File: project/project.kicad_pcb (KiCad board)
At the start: 4 copper layers, 84 x 41 mm, 142 parts, among them J101 Front, J102 FFC, SW101 SW_DIP_x04, U101 GX101, U201 74HC595, U301 74HC595, U401 74HC595, U501 74HC595

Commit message: fixing silkscreen typo
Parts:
- removed kibuzzard-6981884A: G***, kibuzzard-6981884A
- added kibuzzard-698AEBE9: G***, kibuzzard-698AEBE9, B.Cu at (178.3, 105.5)

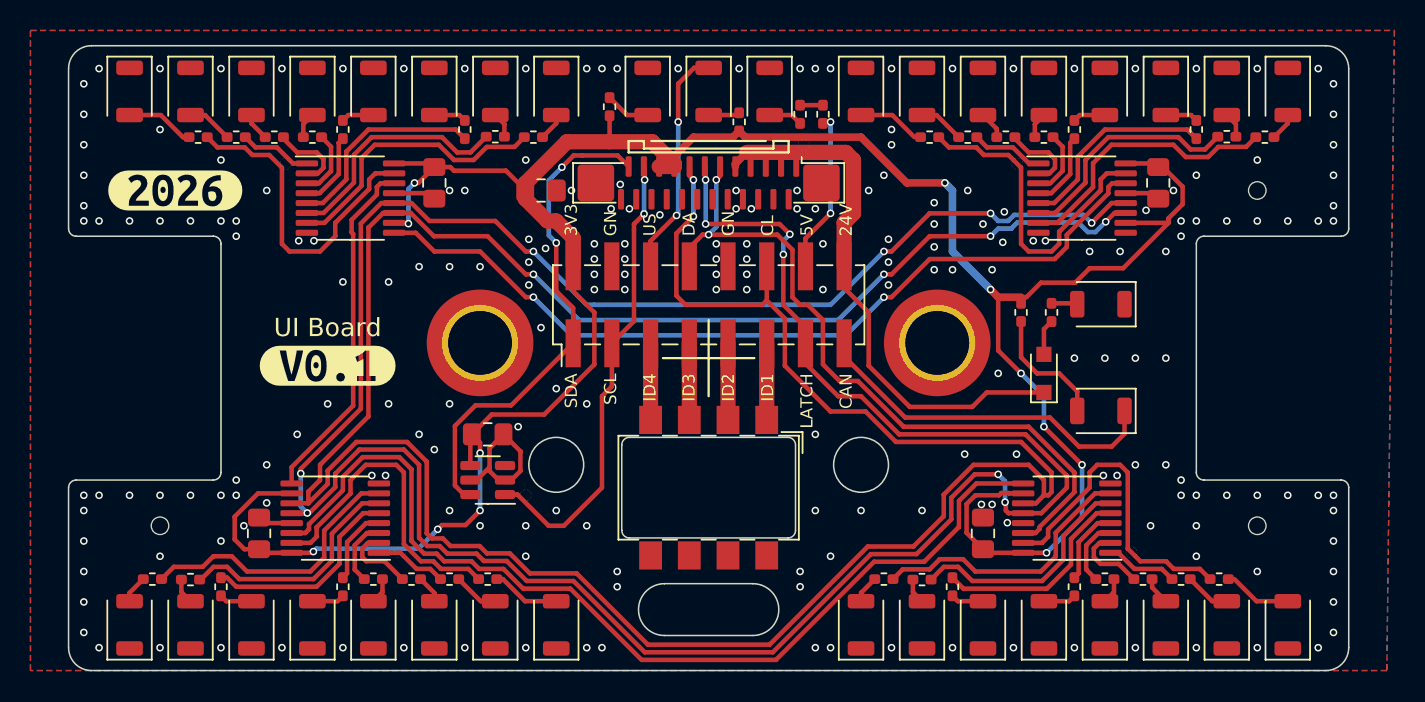
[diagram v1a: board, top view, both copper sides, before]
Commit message: updating kibot,fixing silkscreen, lowering led current
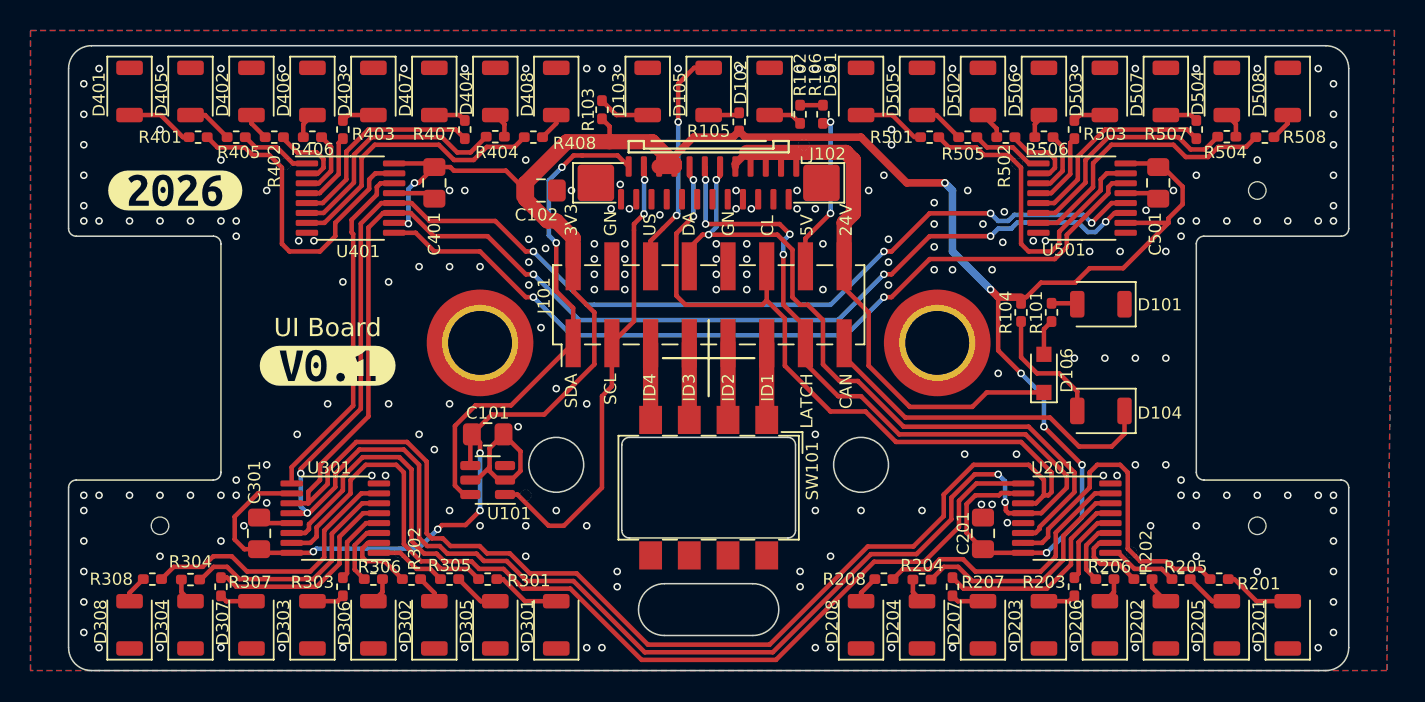
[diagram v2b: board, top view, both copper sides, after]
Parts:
- R201, R202, R203, R204, R205, R206, R207, R208, R301, R302, R303, R304, R305, R306, R307, R308, R401, R402, R403, R404, R405, R406, R407, R408, R501, R502, R503, R504, R505, R506, R507, R508: value 220R -> 330R
- moved R103 0.54 mm to (161.3, 74.7)

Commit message: parts consolidation and small fixes
* Inverting input LEDs
* Switching to TMP102 as TMP101 is no longer available
* Helping 74HC forget state after power loss
* bumping up version
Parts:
- removed REF** (x3): toolhole, -local:toolhole
- removed kibuzzard-69816F1E: G***, kibuzzard-69816F1E
- added R107: 330R, Resistor_SMD:R_0402_1005Metric_Pad0.72x0.64mm_HandSolder, F.Cu at (157.8, 78.8)
- added kibuzzard-69BC5702: G***, kibuzzard-69BC5702, F.Cu at (145.3, 96.0)
- U101: value GX101 -> TMP102; footprint Package_TO_SOT_SMD:SOT-23-6 -> -local:SOT-563
- moved R102 2.55 mm to (174.8, 72.5), turned to 90 degrees
- moved R106 1.00 mm to (174.8, 75.0)
- moved C102 0.50 mm to (157.3, 80.5)
- moved R103 0.23 mm to (161.4, 74.5)
- turned D102 to 90 degrees
- turned D103 to 90 degrees
- turned D105 to 90 degrees
- turned D201 to -90 degrees
- turned D202 to -90 degrees
- turned D203 to -90 degrees
- turned D204 to -90 degrees
- turned D205 to -90 degrees
- turned D206 to -90 degrees
- turned D207 to -90 degrees
- turned D208 to -90 degrees
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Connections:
- D201 pad 1: GND -> /driver1/Ar
- D201 pad 2: /driver1/Ar -> 3V3
- D202 pad 1: GND -> /driver1/Cr
- D202 pad 2: /driver1/Cr -> 3V3
- D203 pad 1: GND -> /driver1/Er
- D203 pad 2: /driver1/Er -> 3V3
- D204 pad 1: GND -> /driver1/Gr
- D204 pad 2: /driver1/Gr -> 3V3
- D205 pad 1: GND -> /driver1/Br
- D205 pad 2: /driver1/Br -> 3V3
- D206 pad 1: GND -> /driver1/Dr
- D206 pad 2: /driver1/Dr -> 3V3
- D207 pad 1: GND -> /driver1/Fr
- D207 pad 2: /driver1/Fr -> 3V3
- D208 pad 1: GND -> /driver1/Hr
- D208 pad 2: /driver1/Hr -> 3V3
- D301 pad 1: GND -> /driver2/Ar
- D301 pad 2: /driver2/Ar -> 3V3
- D302 pad 1: GND -> /driver2/Cr
- D302 pad 2: /driver2/Cr -> 3V3
- D303 pad 1: GND -> /driver2/Er
- D303 pad 2: /driver2/Er -> 3V3
- D304 pad 1: GND -> /driver2/Gr
- D304 pad 2: /driver2/Gr -> 3V3
- D305 pad 1: GND -> /driver2/Br
- D305 pad 2: /driver2/Br -> 3V3
- D306 pad 1: GND -> /driver2/Dr
- D306 pad 2: /driver2/Dr -> 3V3
- D307 pad 1: GND -> /driver2/Fr
- D307 pad 2: /driver2/Fr -> 3V3
- D308 pad 1: GND -> /driver2/Hr
- D308 pad 2: /driver2/Hr -> 3V3
- D401 pad 1: GND -> /driver3/Ar
- D401 pad 2: /driver3/Ar -> 3V3
- D402 pad 1: GND -> /driver3/Cr
- D402 pad 2: /driver3/Cr -> 3V3
- D403 pad 1: GND -> /driver3/Er
- D403 pad 2: /driver3/Er -> 3V3
- D404 pad 1: GND -> /driver3/Gr
- D404 pad 2: /driver3/Gr -> 3V3
- D405 pad 1: GND -> /driver3/Br
- D405 pad 2: /driver3/Br -> 3V3
- D406 pad 1: GND -> /driver3/Dr
- D406 pad 2: /driver3/Dr -> 3V3
- D407 pad 1: GND -> /driver3/Fr
- D407 pad 2: /driver3/Fr -> 3V3
- D408 pad 1: GND -> /driver3/Hr
- D408 pad 2: /driver3/Hr -> 3V3
- D501 pad 1: GND -> /driver4/Ar
- D501 pad 2: /driver4/Ar -> 3V3
- D502 pad 1: GND -> /driver4/Cr
- D502 pad 2: /driver4/Cr -> 3V3
- D503 pad 1: GND -> /driver4/Er
- D503 pad 2: /driver4/Er -> 3V3
- D504 pad 1: GND -> /driver4/Gr
- D504 pad 2: /driver4/Gr -> 3V3
- D505 pad 1: GND -> /driver4/Br
- D505 pad 2: /driver4/Br -> 3V3
- D506 pad 1: GND -> /driver4/Dr
- D506 pad 2: /driver4/Dr -> 3V3
- D507 pad 1: GND -> /driver4/Fr
- D507 pad 2: /driver4/Fr -> 3V3
- D508 pad 1: GND -> /driver4/Hr
- D508 pad 2: /driver4/Hr -> 3V3
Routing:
- net 3V3: track 168.4 -> 311.7 mm, vias 12 -> 14
- net USR_LED: track 15.2 -> 12.4 mm
- net Net-(D105-Pad2): track 2.06 -> 4.34 mm
- net SDA: track 32.7 -> 31.9 mm
- net Net-(D103-Pad2): track 3.39 -> 3.97 mm
- net SCL: track 30.5 -> 31.1 mm
- net GND: track 17.1 -> 17.6 mm, vias 218 -> 189
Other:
- board text added: "WormControl Input32 UI Board"
- board text removed: "UI Board"

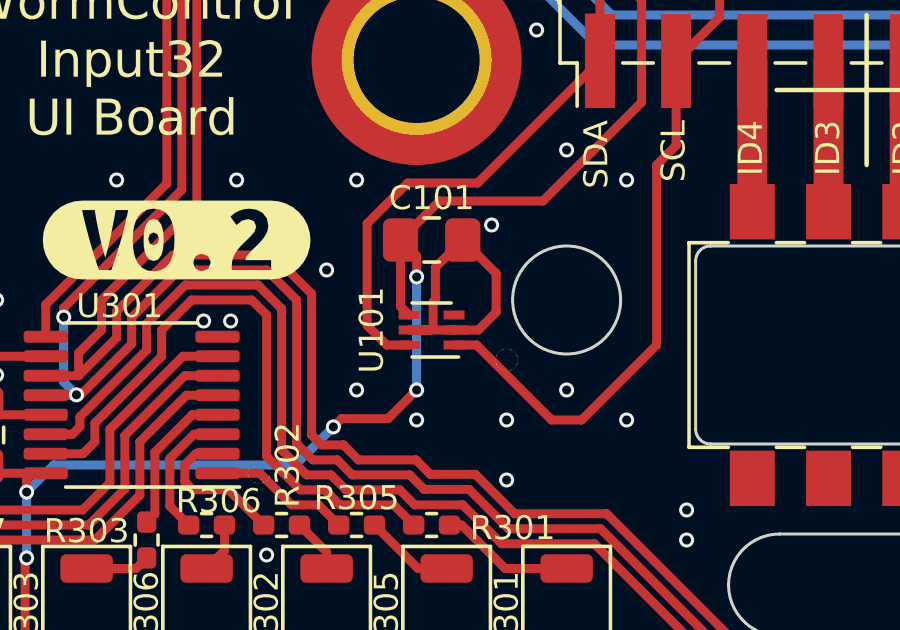
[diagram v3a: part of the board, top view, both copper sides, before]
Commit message: fixing tmp102 pinout
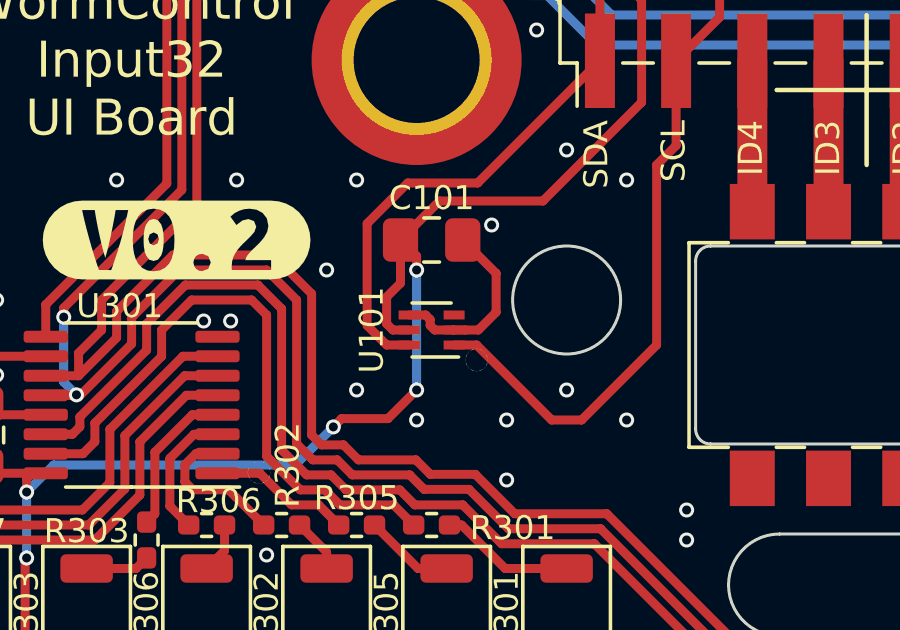
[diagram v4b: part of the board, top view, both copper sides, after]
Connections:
- U101 pad 4: 3V3 -> GND
- U101 pad 5: GND -> 3V3
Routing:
- net GND: track 17.6 -> 13.7 mm
- net 3V3: track 311.7 -> 312.9 mm
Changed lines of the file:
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@@
     )
     (fp_text value "G***" (at 0 4.36087) (layer "F.SilkS") hide
-      (effects (font (size 0 0)))
+      (effects (font (size 0 0) (thickness 0.15)))
     )
     (fp_poly (pts
@@
       (net 1 "unconnected-(U101-Pad3)") (pinfunction "ALERT") (pintype "open_collector+no_connect"))
     (pad "4" smd rect (at 0.75 0.5 180) (size 0.7 0.3) (layers "F.Cu" "F.Paste" "F.Mask")
-      (net 2 "3V3") (pinfunction "V+") (pintype "power_in"))
-    (pad "5" smd rect (at 0.75 0 180) (size 0.7 0.3) (layers "F.Cu" "F.Paste" "F.Mask")
       (net 3 "GND") (pinfunction "ADD0") (pintype "input"))
+    (pad "5" smd rect (at 0.75 0 180) (size 0.7 0.3) (layers "F.Cu" "F.Paste" "F.Mask")
+      (net 2 "3V3") (pinfunction "V+") (pintype "power_in"))
     (pad "6" smd rect (at 0.75 -0.5 180) (size 0.7 0.3) (layers "F.Cu" "F.Paste" "F.Mask")
       (net 45 "SDA") (pinfunction "SDA") (pintype "bidirectional"))
@@
   (gr_line (start 163.0125 76.7875) (end 163.0125 77.5375) (layer "F.SilkS") (width 0.15))
   (gr_circle (center 174.5125 77.0375) (end 174.512501 77.0375) (layer "F.SilkS") (width 0.75) (fill none))
-  (gr_circle (center 156.2625 100.0375) (end 156.262501 100.0375) (layer "F.SilkS") (width 0.75) (fill none))
+  (gr_circle (center 155.2625 100.0375) (end 155.262501 100.0375) (layer "F.SilkS") (width 0.75) (fill none))
   (gr_circle (center 196.0125 103.7875) (end 196.012501 103.7875) (layer "F.SilkS") (width 0.75) (fill none))
   (gr_line (start 172.5125 76.7875) (end 172.5125 77.2875) (layer "F.SilkS") (width 0.15))
@@
     (style (thickness 0.15) (arrow_length 1.27) (text_position_mode 0) (extension_height 0.58642) (extension_offset 0.5) keep_text_aligned)
   )
-  (segment (start 153.2625 96.575) (end 152.725 96.0375) (width 0.3) (layer "F.Cu") (net 2))
   (segment (start 150.2625 110.0875) (end 154.2625 110.0875) (width 0.5) (layer "F.Cu") (net 2))
   (segment (start 187.315656 100.0375) (end 185.7625 100.0375) (width 0.3) (layer "F.Cu") (net 2))
@@
   (segment (start 154.2625 71.9875) (end 158.2625 71.9875) (width 0.5) (layer "F.Cu") (net 2))
   (segment (start 166.0125 77.7875) (end 166.0125 78.4625) (width 0.5) (layer "F.Cu") (net 2))
+  (segment (start 153.2625 97.0375) (end 153.2625 96.575) (width 0.3) (layer "F.Cu") (net 2))
   (segment (start 188.2625 106.762) (end 188.2625 110.0375) (width 0.3) (layer "F.Cu") (net 2))
   (segment (start 138.2625 110.0875) (end 140.2125 110.0875) (width 0.5) (layer "F.Cu") (net 2))
@@
   (segment (start 160.7625 91.4475) (end 160.7625 88.0375) (width 0.3) (layer "F.Cu") (net 2))
   (segment (start 152.725 96.0375) (end 154.025 94.7375) (width 0.3) (layer "F.Cu") (net 2))
+  (segment (start 153.0125 99.0375) (end 152.469606 99.0375) (width 0.3) (layer "F.Cu") (net 2))
   (segment (start 185.1875 100.6125) (end 185.1875 102.5) (width 0.3) (layer "F.Cu") (net 2))
   (segment (start 130.2625 110.0875) (end 134.2625 110.0875) (width 0.5) (layer "F.Cu") (net 2))
@@
   (segment (start 139 103.8125) (end 138.7625 103.575) (width 0.3) (layer "F.Cu") (net 2))
   (segment (start 198.073529 78.5) (end 199.3625 79.788971) (width 0.3) (layer "F.Cu") (net 2))
+  (segment (start 152.469606 99.0375) (end 152.2625 98.830394) (width 0.3) (layer "F.Cu") (net 2))
   (segment (start 161.7625 76.8375) (end 158.633724 76.8375) (width 1) (layer "F.Cu") (net 2))
-  (segment (start 153.2625 97.26875) (end 153.2625 96.575) (width 0.3) (layer "F.Cu") (net 2))
   (segment (start 188.7625 87.0375) (end 187.2625 87.0375) (width 0.5) (layer "F.Cu") (net 2))
   (segment (start 138.7625 103.575) (end 137.8 103.575) (width 0.3) (layer "F.Cu") (net 2))
@@
   (segment (start 142.2625 71.9875) (end 146.2625 71.9875) (width 0.5) (layer "F.Cu") (net 2))
   (segment (start 160.7625 88.0375) (end 159.3725 86.6475) (width 0.3) (layer "F.Cu") (net 2))
+  (segment (start 153.2625 96.575) (end 152.725 96.0375) (width 0.3) (layer "F.Cu") (net 2))
   (segment (start 137.1625 102.9375) (end 137.1625 101.438972) (width 0.3) (layer "F.Cu") (net 2))
   (segment (start 147.625 78.2625) (end 150.025 78.2625) (width 0.3) (layer "F.Cu") (net 2))
   (segment (start 194.2625 110.0875) (end 190.2625 110.0875) (width 0.5) (layer "F.Cu") (net 2))
   (segment (start 175.9625 72.8375) (end 175.9625 76.3375) (width 0.5) (layer "F.Cu") (net 2))
+  (segment (start 152.2625 98.830394) (end 152.2625 97.9375) (width 0.3) (layer "F.Cu") (net 2))
   (segment (start 152.308339 101.991661) (end 150.7625 101.991661) (width 0.3) (layer "F.Cu") (net 2))
   (segment (start 206.2625 71.9875) (end 202.2625 71.9875) (width 0.5) (layer "F.Cu") (net 2))
+  (segment (start 152.725 97.475) (end 152.725 96.0375) (width 0.3) (layer "F.Cu") (net 2))
   (segment (start 140.2625 104.438) (end 140.2625 103.99375) (width 0.3) (layer "F.Cu") (net 2))
   (segment (start 154.9625 78.7375) (end 156.225 80) (width 0.3) (layer "F.Cu") (net 2))
@@
   (segment (start 146.2625 110.0875) (end 150.2625 110.0875) (width 0.5) (layer "F.Cu") (net 2))
   (segment (start 164.5625 76.8375) (end 161.7625 76.8375) (width 1) (layer "F.Cu") (net 2))
-  (segment (start 152.725 98.25) (end 152.725 96.0375) (width 0.3) (layer "F.Cu") (net 2))
+  (segment (start 152.2625 97.9375) (end 152.725 97.475) (width 0.3) (layer "F.Cu") (net 2))
   (segment (start 188.7625 87.0375) (end 189.113972 87.0375) (width 0.3) (layer "F.Cu") (net 2))
   (segment (start 150.2625 71.9875) (end 154.2625 71.9875) (width 0.5) (layer "F.Cu") (net 2))
   (segment (start 188.9 103.8125) (end 186.5 103.8125) (width 0.3) (layer "F.Cu") (net 2))
   (segment (start 186.2625 71.9875) (end 182.2625 71.9875) (width 0.5) (layer "F.Cu") (net 2))
-  (segment (start 153.0125 98.5375) (end 152.725 98.25) (width 0.3) (layer "F.Cu") (net 2))
   (segment (start 187.2625 87.0375) (end 186.7625 86.5375) (width 0.5) (layer "F.Cu") (net 2))
   (segment (start 170.2625 76.135) (end 170.665 76.5375) (width 0.5) (layer "F.Cu") (net 2))
@@
   (via (at 186.7625 86.5375) (size 0.5) (drill 0.3) (layers "F.Cu" "B.Cu") (net 2))
   (via (at 140.2625 104.438) (size 0.5) (drill 0.3) (layers "F.Cu" "B.Cu") (net 2))
-  (via (at 153.2625 97.26875) (size 0.5) (drill 0.3) (layers "F.Cu" "B.Cu") (net 2))
+  (via (at 153.2625 97.0375) (size 0.5) (drill 0.3) (layers "F.Cu" "B.Cu") (net 2))
   (via (at 148.9625 79.5375) (size 0.5) (drill 0.3) (layers "F.Cu" "B.Cu") (net 2))
   (via (at 150.486161 102.268) (size 0.5) (drill 0.3) (layers "F.Cu" "B.Cu") (net 2))
@@
   (segment (start 140.2625 104.438) (end 141.163 103.5375) (width 0.3) (layer "B.Cu") (net 2))
   (segment (start 140.2625 104.438) (end 140.2625 106.637) (width 0.3) (layer "B.Cu") (net 2))
+  (segment (start 153.2625 97.0375) (end 153.2625 101.0375) (width 0.3) (layer "B.Cu") (net 2))
   (segment (start 148.5625 82.213) (end 148.5625 79.9375) (width 0.3) (layer "B.Cu") (net 2))
   (segment (start 149.216661 103.5375) (end 150.486161 102.268) (width 0.3) (layer "B.Cu") (net 2))
-  (segment (start 153.2625 97.26875) (end 153.2625 101.0375) (width 0.3) (layer "B.Cu") (net 2))
   (segment (start 192.7625 101.482572) (end 192.7625 98.0375) (width 0.3) (layer "B.Cu") (net 2))
-  (segment (start 153.8875 98.0375) (end 153.8875 96.95) (width 0.3) (layer "F.Cu") (net 3))
   (segment (start 197.4 80.2125) (end 197.7625 80.575) (width 0.3) (layer "F.Cu") (net 3))
   (segment (start 155.9125 98.444607) (end 155.9125 97.15) (width 0.3) (layer "F.Cu") (net 3))
+  (segment (start 153.7125 98.8875) (end 153.7125 98.6875) (width 0.3) (layer "F.Cu") (net 3))
   (segment (start 154.9 99.0375) (end 154.480393 99.0375) (width 0.3) (layer "F.Cu") (net 3))
-  (segment (start 153.8125 98.9375) (end 153.8125 98.1125) (width 0.3) (layer "F.Cu") (net 3))
   (segment (start 139.125 101.8625) (end 138.7625 101.5) (width 0.3) (layer "F.Cu") (net 3))
   (segment (start 154.9 99.0375) (end 155.319607 99.0375) (width 0.3) (layer "F.Cu") (net 3))
-  (segment (start 153.0125 99.0375) (end 154.5125 99.0375) (width 0.3) (layer "F.Cu") (net 3))
   (segment (start 155.319607 99.0375) (end 155.9125 98.444607) (width 0.3) (layer "F.Cu") (net 3))
   (segment (start 140.9 101.8625) (end 139.125 101.8625) (width 0.3) (layer "F.Cu") (net 3))
-  (segment (start 153.0125 99.0375) (end 153.7125 99.0375) (width 0.3) (layer "F.Cu") (net 3))
   (segment (start 155.9125 97.15) (end 154.8 96.0375) (width 0.3) (layer "F.Cu") (net 3))
-  (segment (start 153.7125 99.0375) (end 153.8125 98.9375) (width 0.3) (layer "F.Cu") (net 3))
+  (segment (start 153.5625 98.5375) (end 153.0125 98.5375) (width 0.3) (layer "F.Cu") (net 3))
+  (segment (start 154.5125 99.0375) (end 153.8625 99.0375) (width 0.3) (layer "F.Cu") (net 3))
   (segment (start 195.625 80.2125) (end 197.4 80.2125) (width 0.3) (layer "F.Cu") (net 3))
   (segment (start 149.9 80.2125) (end 150.2625 80.575) (width 0.3) (layer "F.Cu") (net 3))
-  (segment (start 153.8125 98.1125) (end 153.8875 98.0375) (width 0.3) (layer "F.Cu") (net 3))
-  (segment (start 153.8875 96.95) (end 154.8 96.0375) (width 0.3) (layer "F.Cu") (net 3))
+  (segment (start 153.7125 98.6875) (end 153.5625 98.5375) (width 0.3) (layer "F.Cu") (net 3))
+  (segment (start 153.8625 99.0375) (end 153.7125 98.8875) (width 0.3) (layer "F.Cu") (net 3))
   (segment (start 147.625 80.2125) (end 149.9 80.2125) (width 0.3) (layer "F.Cu") (net 3))
   (via (at 186.8625 100.6375) (size 0.5) (drill 0.3) (layers "F.Cu" "B.Cu") (free) (net 3))
